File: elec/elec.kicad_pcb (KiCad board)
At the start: 2 copper layers, 13 parts, among them J1 BM04B-SRSS-TB, J10 BM04B-SRSS-TB, J11 DB301V-3.5-2P-GN-S, J2 BM04B-SRSS-TB, J3 BM04B-SRSS-TB, J4 BM04B-SRSS-TB, J5 BM04B-SRSS-TB, J6 BM04B-SRSS-TB, J7 BM04B-SRSS-TB, J8 BM04B-SRSS-TB, J9 BM04B-SRSS-TB, SW1 YTSA010

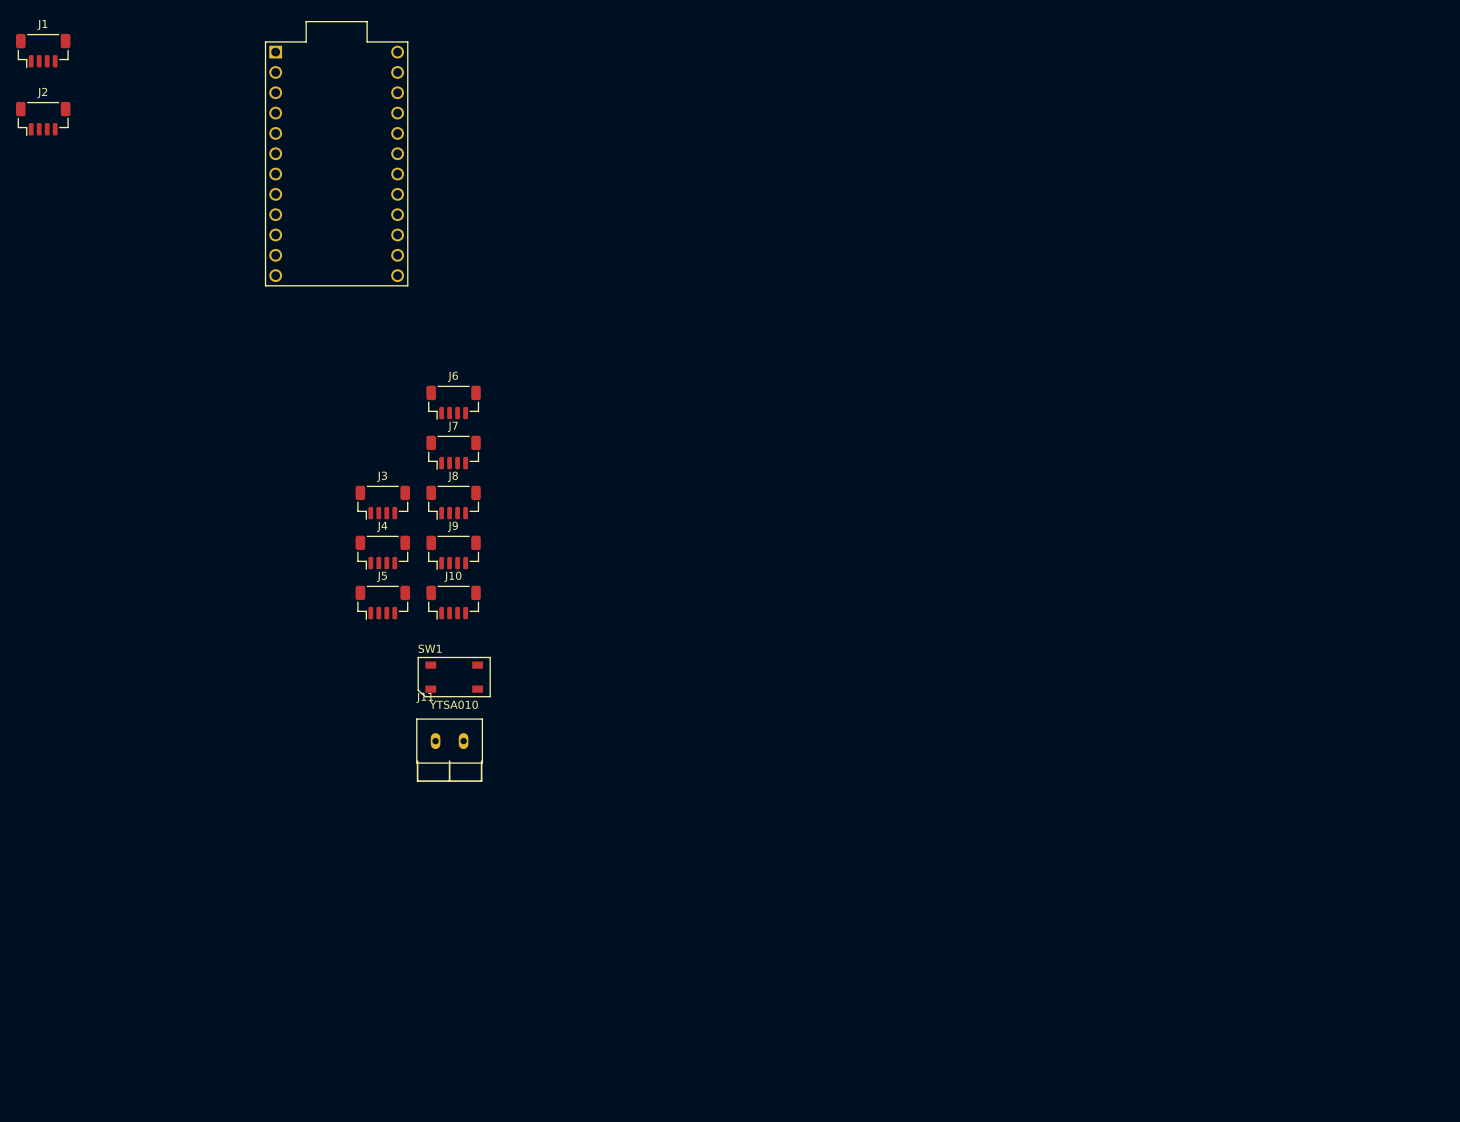
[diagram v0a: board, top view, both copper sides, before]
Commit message: feat: adding modularity to PCB
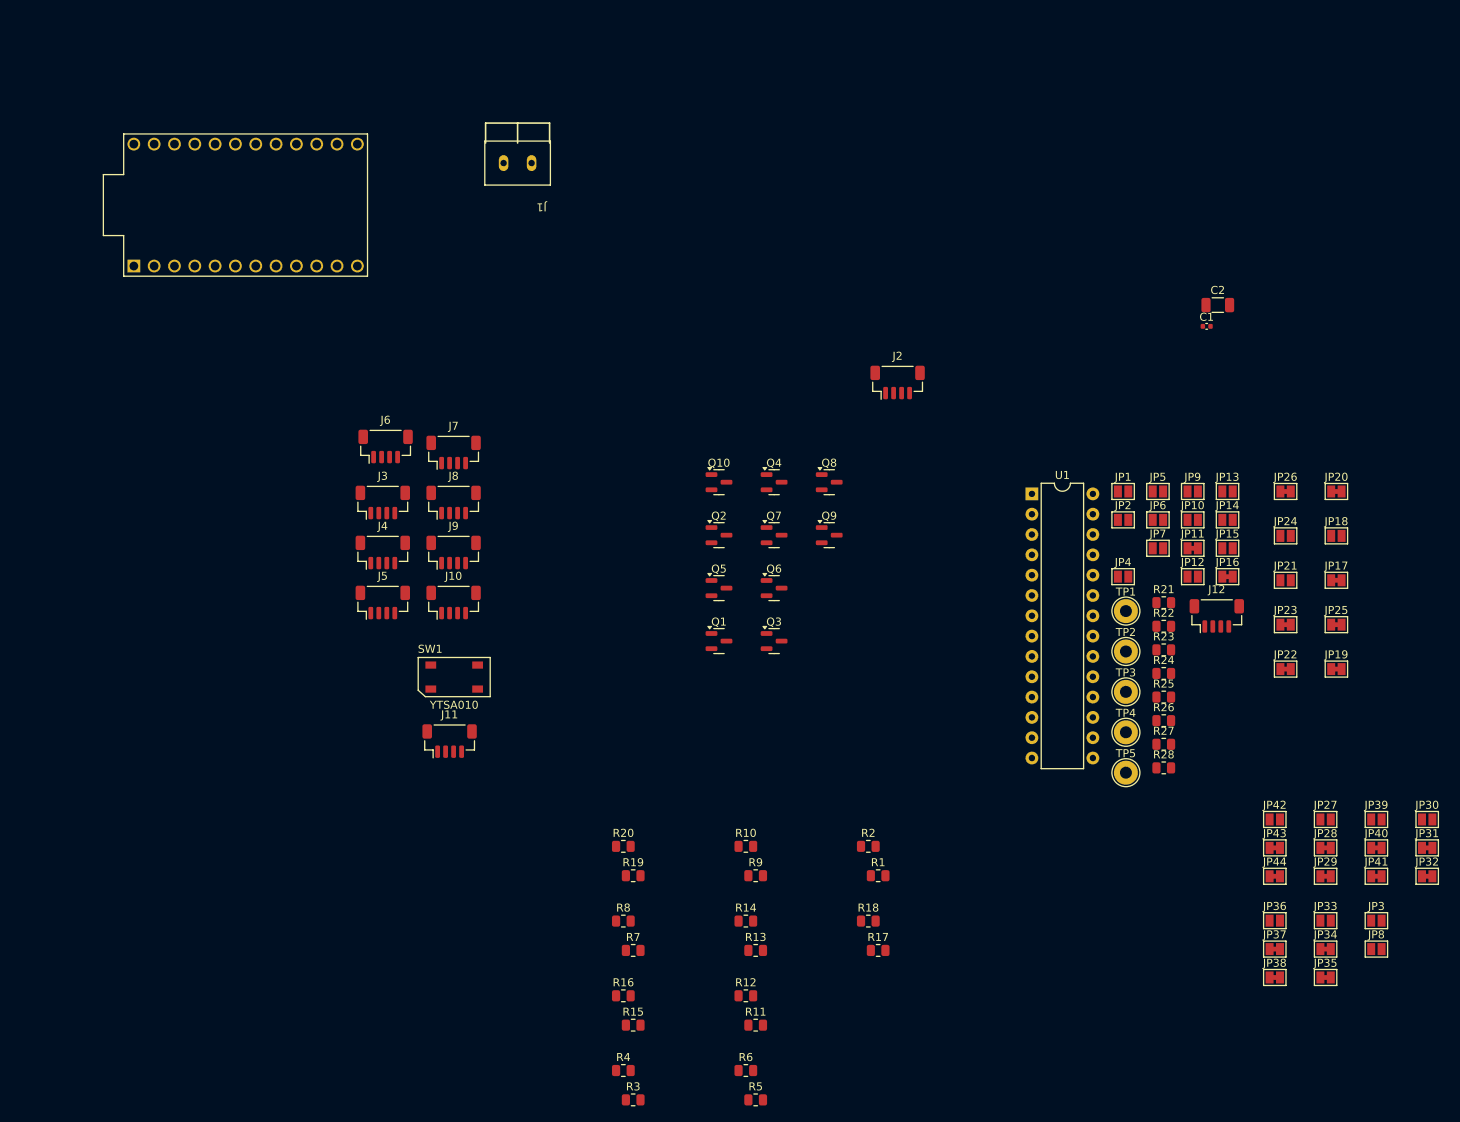
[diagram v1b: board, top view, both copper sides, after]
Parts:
- added C1: 0.1uF, Capacitor_SMD:C_0402_1005Metric, F.Cu at (152.1, 38.7)
- added C2: 10uF, Capacitor_SMD:C_1206_3216Metric, F.Cu at (153.5, 36.0)
- added J12: BM04B-SRSS-TB, jlcpcb:JST_SH_BM04B-SRSS-TB_1x04-1MP_P1.00mm_Vertical, F.Cu at (153.4, 74.8)
- added JP1: SolderJumper_2_Open, Jumper:SolderJumper-2_P1.3mm_Open_Pad1.0x1.5mm, F.Cu at (141.7, 59.3)
- added JP10: SolderJumper_2_Open, Jumper:SolderJumper-2_P1.3mm_Open_Pad1.0x1.5mm, F.Cu at (150.4, 62.9)
- added JP11: SolderJumper_2_Open, Jumper:SolderJumper-2_P1.3mm_Bridged_Pad1.0x1.5mm, F.Cu at (150.4, 66.4)
- added JP12: SolderJumper_2_Open, Jumper:SolderJumper-2_P1.3mm_Open_Pad1.0x1.5mm, F.Cu at (150.4, 70.0)
- added JP13: SolderJumper_2_Open, Jumper:SolderJumper-2_P1.3mm_Open_Pad1.0x1.5mm, F.Cu at (154.7, 59.3)
- added JP14: SolderJumper_2_Open, Jumper:SolderJumper-2_P1.3mm_Open_Pad1.0x1.5mm, F.Cu at (154.7, 62.9)
- added JP15: SolderJumper_2_Open, Jumper:SolderJumper-2_P1.3mm_Open_Pad1.0x1.5mm, F.Cu at (154.7, 66.4)
- added JP16: SolderJumper_2_Bridged, Jumper:SolderJumper-2_P1.3mm_Bridged_Pad1.0x1.5mm, F.Cu at (154.7, 70.0)
- added JP17: SolderJumper_2_Bridged, Jumper:SolderJumper-2_P1.3mm_Bridged_Pad1.0x1.5mm, F.Cu at (168.3, 70.4)
- added JP18: SolderJumper_2_Open, Jumper:SolderJumper-2_P1.3mm_Open_Pad1.0x1.5mm, F.Cu at (168.3, 64.8)
- added JP19: SolderJumper_2_Bridged, Jumper:SolderJumper-2_P1.3mm_Bridged_Pad1.0x1.5mm, F.Cu at (168.3, 81.5)
- added JP2: SolderJumper_2_Open, Jumper:SolderJumper-2_P1.3mm_Open_Pad1.0x1.5mm, F.Cu at (141.7, 62.9)
- added JP20: SolderJumper_2_Bridged, Jumper:SolderJumper-2_P1.3mm_Bridged_Pad1.0x1.5mm, F.Cu at (168.3, 59.3)
- added JP21: SolderJumper_2_Open, Jumper:SolderJumper-2_P1.3mm_Open_Pad1.0x1.5mm, F.Cu at (162.0, 70.4)
- added JP22: SolderJumper_2_Bridged, Jumper:SolderJumper-2_P1.3mm_Bridged_Pad1.0x1.5mm, F.Cu at (162.0, 81.5)
- added JP23: SolderJumper_2_Bridged, Jumper:SolderJumper-2_P1.3mm_Bridged_Pad1.0x1.5mm, F.Cu at (162.0, 76.0)
- added JP24: SolderJumper_2_Open, Jumper:SolderJumper-2_P1.3mm_Open_Pad1.0x1.5mm, F.Cu at (162.0, 64.8)
- added JP25: SolderJumper_2_Bridged, Jumper:SolderJumper-2_P1.3mm_Bridged_Pad1.0x1.5mm, F.Cu at (168.3, 76.0)
- added JP26: SolderJumper_2_Bridged, Jumper:SolderJumper-2_P1.3mm_Bridged_Pad1.0x1.5mm, F.Cu at (162.0, 59.3)
- added JP27: SolderJumper_2_Open, Jumper:SolderJumper-2_P1.3mm_Open_Pad1.0x1.5mm, F.Cu at (167.0, 100.3)
- added JP28: SolderJumper_2_Bridged, Jumper:SolderJumper-2_P1.3mm_Bridged_Pad1.0x1.5mm, F.Cu at (167.0, 103.8)
- added JP29: SolderJumper_2_Bridged, Jumper:SolderJumper-2_P1.3mm_Bridged_Pad1.0x1.5mm, F.Cu at (167.0, 107.4)
- added JP3: SolderJumper_2_Open, Jumper:SolderJumper-2_P1.3mm_Open_Pad1.0x1.5mm, F.Cu at (173.3, 113.0)
- added JP30: SolderJumper_2_Open, Jumper:SolderJumper-2_P1.3mm_Open_Pad1.0x1.5mm, F.Cu at (179.7, 100.3)
- added JP31: SolderJumper_2_Bridged, Jumper:SolderJumper-2_P1.3mm_Bridged_Pad1.0x1.5mm, F.Cu at (179.7, 103.8)
- added JP32: SolderJumper_2_Bridged, Jumper:SolderJumper-2_P1.3mm_Bridged_Pad1.0x1.5mm, F.Cu at (179.7, 107.4)
- added JP33: SolderJumper_2_Open, Jumper:SolderJumper-2_P1.3mm_Open_Pad1.0x1.5mm, F.Cu at (167.0, 113.0)
- added JP34: SolderJumper_2_Bridged, Jumper:SolderJumper-2_P1.3mm_Bridged_Pad1.0x1.5mm, F.Cu at (167.0, 116.5)
- added JP35: SolderJumper_2_Bridged, Jumper:SolderJumper-2_P1.3mm_Bridged_Pad1.0x1.5mm, F.Cu at (167.0, 120.0)
- added JP36: SolderJumper_2_Open, Jumper:SolderJumper-2_P1.3mm_Open_Pad1.0x1.5mm, F.Cu at (160.7, 113.0)
- added JP37: SolderJumper_2_Bridged, Jumper:SolderJumper-2_P1.3mm_Bridged_Pad1.0x1.5mm, F.Cu at (160.7, 116.5)
- added JP38: SolderJumper_2_Bridged, Jumper:SolderJumper-2_P1.3mm_Bridged_Pad1.0x1.5mm, F.Cu at (160.7, 120.0)
- added JP39: SolderJumper_2_Open, Jumper:SolderJumper-2_P1.3mm_Open_Pad1.0x1.5mm, F.Cu at (173.3, 100.3)
- added JP4: SolderJumper_2_Open, Jumper:SolderJumper-2_P1.3mm_Open_Pad1.0x1.5mm, F.Cu at (141.7, 70.0)
- added JP40: SolderJumper_2_Bridged, Jumper:SolderJumper-2_P1.3mm_Bridged_Pad1.0x1.5mm, F.Cu at (173.3, 103.8)
- added JP41: SolderJumper_2_Bridged, Jumper:SolderJumper-2_P1.3mm_Bridged_Pad1.0x1.5mm, F.Cu at (173.3, 107.4)
- added JP42: SolderJumper_2_Open, Jumper:SolderJumper-2_P1.3mm_Open_Pad1.0x1.5mm, F.Cu at (160.7, 100.3)
- added JP43: SolderJumper_2_Bridged, Jumper:SolderJumper-2_P1.3mm_Bridged_Pad1.0x1.5mm, F.Cu at (160.7, 103.8)
- added JP44: SolderJumper_2_Bridged, Jumper:SolderJumper-2_P1.3mm_Bridged_Pad1.0x1.5mm, F.Cu at (160.7, 107.4)
- added JP5: SolderJumper_2_Open, Jumper:SolderJumper-2_P1.3mm_Open_Pad1.0x1.5mm, F.Cu at (146.0, 59.3)
- added JP6: SolderJumper_2_Open, Jumper:SolderJumper-2_P1.3mm_Open_Pad1.0x1.5mm, F.Cu at (146.0, 62.9)
- added JP7: SolderJumper_2_Open, Jumper:SolderJumper-2_P1.3mm_Open_Pad1.0x1.5mm, F.Cu at (146.0, 66.4)
- added JP8: SolderJumper_2_Open, Jumper:SolderJumper-2_P1.3mm_Open_Pad1.0x1.5mm, F.Cu at (173.3, 116.5)
- added JP9: SolderJumper_2_Open, Jumper:SolderJumper-2_P1.3mm_Open_Pad1.0x1.5mm, F.Cu at (150.4, 59.3)
- added Q1: 2N7002, Package_TO_SOT_SMD:SOT-23, F.Cu at (91.2, 78.0)
- added Q10: 2N7002, Package_TO_SOT_SMD:SOT-23, F.Cu at (91.2, 58.1)
- added Q2: 2N7002, Package_TO_SOT_SMD:SOT-23, F.Cu at (91.2, 64.8)
- added Q3: 2N7002, Package_TO_SOT_SMD:SOT-23, F.Cu at (98.1, 78.0)
- added Q4: 2N7002, Package_TO_SOT_SMD:SOT-23, F.Cu at (98.1, 58.1)
- added Q5: 2N7002, Package_TO_SOT_SMD:SOT-23, F.Cu at (91.2, 71.4)
- added Q6: 2N7002, Package_TO_SOT_SMD:SOT-23, F.Cu at (98.1, 71.4)
- added Q7: 2N7002, Package_TO_SOT_SMD:SOT-23, F.Cu at (98.1, 64.8)
- added Q8: 2N7002, Package_TO_SOT_SMD:SOT-23, F.Cu at (105.0, 58.1)
- added Q9: 2N7002, Package_TO_SOT_SMD:SOT-23, F.Cu at (105.0, 64.8)
- added R1: 10k, Resistor_SMD:R_0805_2012Metric, F.Cu at (111.1, 107.3)
- added R10: 1k, Resistor_SMD:R_0805_2012Metric, F.Cu at (94.5, 103.7)
- added R11: 10k, Resistor_SMD:R_0805_2012Metric, F.Cu at (95.8, 126.0)
- added R12: 1k, Resistor_SMD:R_0805_2012Metric, F.Cu at (94.5, 122.3)
- added R13: 10k, Resistor_SMD:R_0805_2012Metric, F.Cu at (95.8, 116.7)
- added R14: 1k, Resistor_SMD:R_0805_2012Metric, F.Cu at (94.5, 113.0)
- added R15: 10k, Resistor_SMD:R_0805_2012Metric, F.Cu at (80.5, 126.0)
- added R16: 1k, Resistor_SMD:R_0805_2012Metric, F.Cu at (79.2, 122.3)
- added R17: 10k, Resistor_SMD:R_0805_2012Metric, F.Cu at (111.1, 116.7)
- added R18: 1k, Resistor_SMD:R_0805_2012Metric, F.Cu at (109.8, 113.0)
- added R19: 10k, Resistor_SMD:R_0805_2012Metric, F.Cu at (80.5, 107.3)
- added R2: 10k, Resistor_SMD:R_0805_2012Metric, F.Cu at (109.8, 103.7)
- added R20: 1k, Resistor_SMD:R_0805_2012Metric, F.Cu at (79.2, 103.7)
- added R21: 10k, Resistor_SMD:R_0805_2012Metric, F.Cu at (146.8, 73.2)
- added R22: 1k, Resistor_SMD:R_0805_2012Metric, F.Cu at (146.8, 76.2)
- added R23: 10k, Resistor_SMD:R_0805_2012Metric, F.Cu at (146.8, 79.1)
- added R24: 1k, Resistor_SMD:R_0805_2012Metric, F.Cu at (146.8, 82.0)
- added R25: 10k, Resistor_SMD:R_0805_2012Metric, F.Cu at (146.8, 85.0)
- added R26: 1k, Resistor_SMD:R_0805_2012Metric, F.Cu at (146.8, 88.0)
- added R27: 10k, Resistor_SMD:R_0805_2012Metric, F.Cu at (146.8, 90.9)
- added R28: 1k, Resistor_SMD:R_0805_2012Metric, F.Cu at (146.8, 93.8)
- added R3: 10k, Resistor_SMD:R_0805_2012Metric, F.Cu at (80.5, 135.3)
- added R4: 10k, Resistor_SMD:R_0805_2012Metric, F.Cu at (79.2, 131.7)
- added R5: 10k, Resistor_SMD:R_0805_2012Metric, F.Cu at (95.8, 135.3)
- added R6: 10k, Resistor_SMD:R_0805_2012Metric, F.Cu at (94.5, 131.7)
- added R7: 4.7k, Resistor_SMD:R_0805_2012Metric, F.Cu at (80.5, 116.7)
- added R8: 4.7k, Resistor_SMD:R_0805_2012Metric, F.Cu at (79.2, 113.0)
- added R9: 10k, Resistor_SMD:R_0805_2012Metric, F.Cu at (95.8, 107.3)
- added TP1: TestPoint_Probe, TestPoint:TestPoint_THTPad_D3.0mm_Drill1.5mm, F.Cu at (142.0, 74.2)
- added TP2: TestPoint_Probe, TestPoint:TestPoint_THTPad_D3.0mm_Drill1.5mm, F.Cu at (142.0, 79.3)
- added TP3: TestPoint_Probe, TestPoint:TestPoint_THTPad_D3.0mm_Drill1.5mm, F.Cu at (142.0, 84.3)
- added TP4: TestPoint_Probe, TestPoint:TestPoint_THTPad_D3.0mm_Drill1.5mm, F.Cu at (142.0, 89.4)
- added TP5: TestPoint_Probe, TestPoint:TestPoint_THTPad_D3.0mm_Drill1.5mm, F.Cu at (142.0, 94.5)
- added U1: MCP23017_SP, Package_DIP:DIP-28_W7.62mm, F.Cu at (130.3, 59.6)
- J1: value BM04B-SRSS-TB -> DB301V-3.5-2P-GN-S; footprint jlcpcb:JST_SH_BM04B-SRSS-TB_1x04-1MP_P1.00mm_Vertical -> jlcpcb:DB301V-3.5-2P-GN-S
- J11: value DB301V-3.5-2P-GN-S -> BM04B-SRSS-TB; footprint jlcpcb:DB301V-3.5-2P-GN-S -> jlcpcb:JST_SH_BM04B-SRSS-TB_1x04-1MP_P1.00mm_Vertical
- moved J2 111.8 mm to (113.5, 45.7)
- moved J1 60.9 mm to (66.0, 18.2), turned to 180 degrees
- moved MCU1 12.5 mm to (32.0, 23.5), turned to 0 degrees
- moved J6 10.1 mm to (49.5, 53.7)
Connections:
- J1 pad 1: +5V -> +24V
- J1 pad 2: /BTN1 -> GND
- J10 pad 1: +5V -> GND
- J10 pad 2: /BTN10 -> /BTN8
- J10 pad 3: GND -> /switch_connector8/CONN
- J11 pad 1: +24V -> GND
- J11 pad 2: GND -> /BTN10
- J2 pad 1: +5V -> Net-(J2-Pin_1)
- J2 pad 2: /BTN2 -> Net-(J2-Pin_2)
- J2 pad 3: GND -> +5V
- J2 pad 4: +24V -> GND
- J3 pad 1: +5V -> GND
- J3 pad 2: /BTN3 -> /BTN1
- J3 pad 3: GND -> /switch_connector1/CONN
- J4 pad 1: +5V -> GND
- J4 pad 2: /BTN4 -> /BTN2
- J4 pad 3: GND -> /switch_connector2/CONN
- J5 pad 1: +5V -> GND
- J5 pad 2: /BTN5 -> /BTN3
- J5 pad 3: GND -> /switch_connector3/CONN
- J6 pad 1: +5V -> GND
- J6 pad 2: /BTN6 -> /BTN4
- J6 pad 3: GND -> /switch_connector4/CONN
- J7 pad 1: +5V -> GND
- J7 pad 2: /BTN7 -> /BTN5
- J7 pad 3: GND -> /switch_connector5/CONN
- J8 pad 1: +5V -> GND
- J8 pad 2: /BTN8 -> /BTN6
- J8 pad 3: GND -> /switch_connector6/CONN
- J9 pad 1: +5V -> GND
- J9 pad 2: /BTN9 -> /BTN7
- J9 pad 3: GND -> /switch_connector7/CONN
- MCU1 pad 13: /BTN10 -> /LA1
- MCU1 pad 14: /BTN9 -> /LA2
- MCU1 pad 15: /BTN8 -> /LA3
- MCU1 pad 16: /BTN7 -> /LA4
- MCU1 pad 17: /BTN6 -> /LA5
- MCU1 pad 18: unconnected-(MCU1-A1-Pad18) -> /LA6
- MCU1 pad 19: unconnected-(MCU1-A2-Pad19) -> /BTN10
- MCU1 pad 20: unconnected-(MCU1-A3-Pad20) -> /LA10
- MCU1 pad 5: unconnected-(MCU1-2-Pad5) -> /SDA
- MCU1 pad 6: unconnected-(MCU1-3-Pad6) -> /SCL
- MCU1 pad 7: unconnected-(MCU1-4-Pad7) -> /BTN6

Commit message: v1 3D print PCB
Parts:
- removed JP35, JP37, JP38, JP40, JP41, JP43, JP44: SolderJumper_2_Bridged, Jumper:SolderJumper-2_P1.3mm_Bridged_Pad1.0x1.5mm
- removed JP36, JP39, JP42: SolderJumper_2_Open, Jumper:SolderJumper-2_P1.3mm_Open_Pad1.0x1.5mm
- added REF**: MountingHole_2.2mm_M2_ISO14580_Pad_TopBottom, MountingHole:MountingHole_2.2mm_M2_ISO14580_Pad_TopBottom, F.Cu at (23.0, 102.0)
- added REF**: MountingHole_2.2mm_M2_ISO14580_Pad_TopBottom, MountingHole:MountingHole_2.2mm_M2_ISO14580_Pad_TopBottom, F.Cu at (23.0, 22.0)
- added REF**: MountingHole_2.2mm_M2_ISO14580_Pad_TopBottom, MountingHole:MountingHole_2.2mm_M2_ISO14580_Pad_TopBottom, F.Cu at (151.0, 22.0)
- added REF**: MountingHole_2.2mm_M2_ISO14580_Pad_TopBottom, MountingHole:MountingHole_2.2mm_M2_ISO14580_Pad_TopBottom, F.Cu at (151.0, 102.0)
- JP1, JP2, JP3, JP4, JP5, JP6: moved to B.Cu
- JP15, JP21, JP27, JP33: value SolderJumper_2_Open -> SolderJumper_2_Bridged; footprint Jumper:SolderJumper-2_P1.3mm_Open_Pad1.0x1.5mm -> Jumper:SolderJumper-2_P1.3mm_Bridged_Pad1.0x1.5mm
- JP16, JP20, JP22, JP26, JP28, JP32, JP34: value SolderJumper_2_Bridged -> SolderJumper_2_Open; footprint Jumper:SolderJumper-2_P1.3mm_Bridged_Pad1.0x1.5mm -> Jumper:SolderJumper-2_P1.3mm_Open_Pad1.0x1.5mm
- moved JP17 137.8 mm to (32.4, 47.9), turned to 180 degrees
- moved JP19 137.6 mm to (32.4, 60.1), turned to 180 degrees
- moved JP18 133.8 mm to (35.9, 45.8)
- moved JP20 132.4 mm to (36.0, 58.0)
- moved JP23 129.9 mm to (32.4, 84.3), turned to 180 degrees
- moved JP21 129.6 mm to (32.4, 72.1), turned to 180 degrees
- moved JP24 127.3 mm to (35.9, 82.2)
- moved JP22 126.5 mm to (36.0, 70.1)
- moved JP15 126.0 mm to (32.5, 35.8), turned to 180 degrees
- moved JP16 124.3 mm to (35.9, 33.5)
- moved R12 98.8 mm to (32.4, 45.5)
- moved R11 97.6 mm to (39.8, 46.1), turned to 90 degrees
- moved TP2 96.2 mm to (54.2, 40.0)
- moved TP1 95.5 mm to (56.8, 31.2)
- moved R10 93.8 mm to (32.4, 33.4)
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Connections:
- J1 pad 1: +24V -> GND
- J1 pad 2: GND -> +24V
- J11 pad 2: /BTN10 -> /BTN9
- J11 pad 3: /switch_connector10/CONN -> /switch_connector9/CONN
- J12 pad 2: /BTN9 -> /BTN10
- J12 pad 3: /switch_connector9/CONN -> /switch_connector10/CONN
- JP15 pad 1: /switch_connector1/CONN -> Net-(JP15-A)
- JP15 pad 2: GND -> /switch_connector1/CONN
- JP16 pad 1: Net-(JP16-A) -> Net-(JP15-A)
- JP16 pad 2: /switch_connector1/CONN -> GND
- JP17 pad 2: Net-(JP16-A) -> /switch_connector2/CONN
- JP18 pad 1: /switch_connector2/CONN -> Net-(JP17-A)
- JP19 pad 2: /switch_connector2/CONN -> /switch_connector3/CONN
- JP20 pad 1: Net-(JP20-A) -> Net-(JP19-A)
- JP20 pad 2: Net-(JP19-A) -> GND
- JP21 pad 1: /switch_connector3/CONN -> Net-(JP21-A)
- JP21 pad 2: GND -> /switch_connector4/CONN
- JP22 pad 1: Net-(JP22-A) -> Net-(JP21-A)
- JP22 pad 2: /switch_connector3/CONN -> GND
- JP23 pad 2: Net-(JP22-A) -> /switch_connector5/CONN
- JP24 pad 1: /switch_connector4/CONN -> Net-(JP23-A)
- JP25 pad 2: /switch_connector4/CONN -> /switch_connector6/CONN
- JP26 pad 1: Net-(JP26-A) -> Net-(JP25-A)
- JP26 pad 2: Net-(JP25-A) -> GND
- JP27 pad 1: /switch_connector5/CONN -> Net-(JP27-A)
- JP27 pad 2: GND -> /switch_connector7/CONN
- JP28 pad 1: Net-(JP28-A) -> Net-(JP27-A)
- JP28 pad 2: /switch_connector5/CONN -> GND
- JP29 pad 2: Net-(JP28-A) -> /switch_connector8/CONN
- JP30 pad 1: /switch_connector6/CONN -> Net-(JP29-A)
- JP31 pad 2: /switch_connector6/CONN -> /switch_connector9/CONN
- JP32 pad 1: Net-(JP32-A) -> Net-(JP31-A)
- JP32 pad 2: Net-(JP31-A) -> GND
- JP33 pad 1: /switch_connector7/CONN -> Net-(JP33-A)
- JP33 pad 2: GND -> /switch_connector10/CONN
- JP34 pad 1: Net-(JP34-A) -> Net-(JP33-A)
- JP34 pad 2: /switch_connector7/CONN -> GND
- JP4 pad 1: /BTN9 -> /LA6
- JP4 pad 2: /BTN10 -> /LA7
- JP5 pad 2: /BTN8 -> /BTN10
- JP6 pad 1: /BTN7 -> /BTN9
- MCU1 pad 10: /BTN3 -> /BTN6
- MCU1 pad 11: /BTN1 -> /BTN5
- MCU1 pad 12: /BTN2 -> /LA5
- MCU1 pad 14: /LA2 -> /BTN1
- MCU1 pad 15: /LA3 -> /LA2
- MCU1 pad 16: /LA4 -> /BTN2
- MCU1 pad 17: /LA5 -> /LA3
- MCU1 pad 18: /LA6 -> /BTN3
- MCU1 pad 19: /BTN10 -> /LA4
- MCU1 pad 20: /LA10 -> /BTN4
- MCU1 pad 3: unconnected-(MCU1-GND-Pad3) -> GND
- MCU1 pad 4: unconnected-(MCU1-GND-Pad4) -> GND
- MCU1 pad 7: /BTN6 -> /LA10
- MCU1 pad 8: /BTN5 -> /BTN10
- MCU1 pad 9: /BTN4 -> /BTN7
- Q1 pad 3: Net-(JP17-A) -> Net-(JP15-A)
- Q10 pad 1: /LA9 -> /LA10
- Q10 pad 3: Net-(JP44-A) -> Net-(JP33-A)
- Q2 pad 3: Net-(JP20-A) -> Net-(JP17-A)
- Q3 pad 3: Net-(JP23-A) -> Net-(JP19-A)
- Q4 pad 3: Net-(JP26-A) -> Net-(JP21-A)
- Q5 pad 3: Net-(JP29-A) -> Net-(JP23-A)
- Q6 pad 3: Net-(JP32-A) -> Net-(JP25-A)
- Q7 pad 3: Net-(JP35-A) -> Net-(JP27-A)
- Q8 pad 3: Net-(JP38-A) -> Net-(JP29-A)
- Q9 pad 1: /LA10 -> /LA9
- Q9 pad 3: Net-(JP41-A) -> Net-(JP31-A)
- R10 pad 1: Net-(JP16-A) -> /switch_connector1/CONN
- R10 pad 2: Net-(JP17-A) -> Net-(JP15-A)
- R12 pad 1: Net-(JP19-A) -> /switch_connector2/CONN
- R12 pad 2: Net-(JP20-A) -> Net-(JP17-A)
- R14 pad 1: Net-(JP22-A) -> /switch_connector3/CONN
- R14 pad 2: Net-(JP23-A) -> Net-(JP19-A)
- R16 pad 1: Net-(JP25-A) -> /switch_connector4/CONN
- R16 pad 2: Net-(JP26-A) -> Net-(JP21-A)
- R18 pad 1: Net-(JP28-A) -> /switch_connector5/CONN
- R18 pad 2: Net-(JP29-A) -> Net-(JP23-A)
- R20 pad 1: Net-(JP31-A) -> /switch_connector6/CONN
- R20 pad 2: Net-(JP32-A) -> Net-(JP25-A)
- R22 pad 1: Net-(JP34-A) -> /switch_connector7/CONN
- R22 pad 2: Net-(JP35-A) -> Net-(JP27-A)
- R24 pad 1: Net-(JP37-A) -> /switch_connector8/CONN
- R24 pad 2: Net-(JP38-A) -> Net-(JP29-A)
- R25 pad 1: /LA10 -> /LA9
- R26 pad 1: Net-(JP40-A) -> /switch_connector9/CONN
- R26 pad 2: Net-(JP41-A) -> Net-(JP31-A)
- R27 pad 1: /LA9 -> /LA10
- R28 pad 1: Net-(JP43-A) -> /switch_connector10/CONN
- R28 pad 2: Net-(JP44-A) -> Net-(JP33-A)
- U1 pad 1: /BTN6 -> /LA6
- U1 pad 2: /BTN7 -> /BTN6
- U1 pad 21: /LA9 -> /LA10
- U1 pad 22: /LA10 -> /BTN10
- U1 pad 23: unconnected-(U1-GPA2-Pad23) -> /LA9
- U1 pad 24: unconnected-(U1-GPA3-Pad24) -> /BTN9
- U1 pad 25: unconnected-(U1-GPA4-Pad25) -> /LA8
- U1 pad 26: unconnected-(U1-GPA5-Pad26) -> /BTN8
- U1 pad 27: unconnected-(U1-GPA6-Pad27) -> /LA7
- U1 pad 28: unconnected-(U1-GPA7-Pad28) -> /BTN7
- U1 pad 3: /BTN8 -> unconnected-(U1-GPB2-Pad3)
- U1 pad 4: /BTN9 -> unconnected-(U1-GPB3-Pad4)
- U1 pad 5: /BTN10 -> unconnected-(U1-GPB4-Pad5)
- U1 pad 6: /LA6 -> unconnected-(U1-GPB5-Pad6)
- U1 pad 7: /LA7 -> unconnected-(U1-GPB6-Pad7)
- U1 pad 8: /LA8 -> unconnected-(U1-GPB7-Pad8)
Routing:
- net +24V: track 0.00 -> 394.1 mm
- net +5V: track 0.00 -> 182.9 mm, vias 0 -> 2
- net /BTN10: track 0.00 -> 117.5 mm, vias 0 -> 3
- net /LA10: track 0.00 -> 115.2 mm, vias 0 -> 3
- net /BTN7: track 0.00 -> 103.4 mm, vias 0 -> 2
- net /BTN6: track 0.00 -> 101.3 mm
- net /BTN5: track 0.00 -> 91.4 mm
- net /LA5: track 0.00 -> 81.5 mm
- net GND: track 0.00 -> 78.1 mm, vias 0 -> 69
- net /LA6: track 0.00 -> 59.5 mm, vias 0 -> 1
- net /BTN9: track 0.00 -> 49.3 mm, vias 0 -> 2
- net Net-(JP10-B): track 0.00 -> 45.4 mm
- net /LA1: track 0.00 -> 44.8 mm
- net /BTN4: track 0.00 -> 44.8 mm
- net Net-(U1-INTA): track 0.00 -> 44.5 mm
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- added copper zone on B.Cu, net GND
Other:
- board outline added: 141 x 93 mm

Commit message: doc: outline for fabrication guide
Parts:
- J1: value DB301V-3.5-2P-GN-S -> Screw terminal
- JP11: footprint Jumper:SolderJumper-2_P1.3mm_Bridged_Pad1.0x1.5mm -> Jumper:SolderJumper-2_P1.3mm_Open_Pad1.0x1.5mm
- moved JP10 2.51 mm to (109.8, 98.8)
- moved R4 2.51 mm to (109.8, 96.2)
- moved C1 0.54 mm to (101.0, 66.3)
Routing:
- net GND: track 78.1 -> 73.3 mm, vias 69 -> 107
- net Net-(JP10-B): track 45.4 -> 44.9 mm
- added copper zone on F.Cu, net GND

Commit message: main - feat: updating delivrables
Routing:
- net GND: vias 107 -> 110
